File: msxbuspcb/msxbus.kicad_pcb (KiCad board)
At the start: 2 copper layers, 9 parts, among them J1 RPi_GPIO, P1 CONN_02X25, P2 CONN_02X25, P4 CONN_01X03, U1 EMP240

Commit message: route for pcb
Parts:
- added P3: CONN_02X05, Pin_Headers:Pin_Header_Straight_2x05, F.Cu at (167.6, 100.4)
- R1, R2, R3, R4: footprint Resistors_SMD:R_2010_HandSoldering -> Resistors_SMD:R_0603_HandSoldering
- moved R1 15.7 mm to (168.9, 97.2)
- moved R2 15.0 mm to (173.3, 100.9), turned to 270 degrees
- moved R3 14.2 mm to (173.3, 105.6), turned to 90 degrees
- moved R4 13.5 mm to (173.4, 110.4), turned to 270 degrees
- moved P4 2.36 mm to (110.5, 94.0)
- moved U1 2.34 mm to (143.3, 105.9)
- moved P2 1.80 mm to (172.1, 146.7)
- moved P1 1.80 mm to (172.1, 125.1)
- moved J1 0.90 mm to (167.6, 80.0)
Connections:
- net /3V3 renamed +3V3
- net /CLK3 renamed Net-(U1-Pad64)
- J1 pad 15: /SLTSL1 -> /MSLTSL1
- U1 pad 100: /SLTSL0 -> /SLTSL1
- U1 pad 30: /MD11 -> Net-(U1-Pad30)
- U1 pad 33: /MD08 -> /MD11
- U1 pad 34: /MD11 -> /MD08
- U1 pad 49: Net-(U1-Pad49) -> /SW2
- U1 pad 50: Net-(U1-Pad50) -> /SW1
- U1 pad 51: /SW2 -> /SWOUT
- U1 pad 52: /SW1 -> /CLOCK
- U1 pad 53: /SWOUT -> /D7
- U1 pad 54: /D7 -> /D6
- U1 pad 55: /D6 -> /D5
- U1 pad 56: /D5 -> /D4
- U1 pad 57: /D4 -> /D3
- U1 pad 58: /D3 -> /D2
- U1 pad 61: /D2 -> /D1
- U1 pad 62: /CLOCK -> /D0
- U1 pad 66: /D1 -> /A5
- U1 pad 67: /D0 -> /A4
- U1 pad 68: /A5 -> /A3
- U1 pad 97: /CS1 -> /SLTSL0
- U1 pad 98: /CS2 -> /CS1
- U1 pad 99: /SLTSL1 -> /CS2
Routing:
- net +3V3: track 0.00 -> 159.3 mm, vias 0 -> 3
- net +5V: track 0.00 -> 149.4 mm
- net /SW2: track 0.00 -> 69.8 mm
- net /SLTSL1: track 0.00 -> 63.2 mm
- net Net-(P2-Pad49): track 0.00 -> 58.9 mm
- net /CS2: track 0.00 -> 56.9 mm
- net /CS1: track 0.00 -> 52.0 mm
- net /RFSH: track 0.00 -> 51.3 mm
- net /CS12: track 0.00 -> 49.5 mm
- net /INT: track 0.00 -> 49.4 mm
- net /CLOCK: track 0.00 -> 48.6 mm
- net /D6: track 0.00 -> 47.2 mm
- net /BUSDIR: track 0.00 -> 47.1 mm
- net /D4: track 0.00 -> 45.8 mm
- net /MERQ: track 0.00 -> 45.4 mm
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- added copper zone on F.Cu, net /GND
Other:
- board outline added: 72.4 x 77.5 mm
- net class 3V3 added: clearance 0.18, trace_width 0.2, via_dia 0.6, via_drill 0.4
- net class 5V added: clearance 0.18, trace_width 0.5, via_dia 0.6, via_drill 0.4
- net class Default: clearance 0.2 -> 0.18; trace_width 0.25 -> 0.2
- rule trace_clearance: 0.2 -> 0.18

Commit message: simple PCB added
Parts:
- added G***: LOGO, msxbuspcb:msx, F.Cu at (99.6, 123.4)
- moved R3 31.3 mm to (163.8, 75.8)
- moved U1 31.3 mm to (133.7, 76.1)
- moved J1 31.3 mm to (158.1, 50.2)
- moved P1 31.3 mm to (162.6, 95.2)
- moved P2 31.3 mm to (162.6, 116.8)
- moved P3 31.3 mm to (158.1, 70.6)
- moved P4 31.3 mm to (101.0, 64.1)
- moved R2 31.3 mm to (163.8, 71.0)
- moved R4 31.3 mm to (163.9, 80.6)
- moved R1 31.3 mm to (159.3, 67.4)
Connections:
- net Net-(P1-Pad49) renamed /SOUNDIN1
- net Net-(P2-Pad49) renamed /SOUNDIN0
- J1 pad 14: /GND -> GND
- J1 pad 20: /GND -> GND
- J1 pad 25: /GND -> GND
- J1 pad 30: /GND -> GND
- J1 pad 34: /GND -> GND
- J1 pad 39: /GND -> GND
- J1 pad 6: /GND -> GND
- J1 pad 9: /GND -> GND
- P1 pad 41: /GND -> GND
- P1 pad 43: /GND -> GND
- P1 pad 47: Net-(P1-Pad47) -> +5V
- P2 pad 41: /GND -> GND
- P2 pad 43: /GND -> GND
- P2 pad 47: Net-(P2-Pad47) -> +5V
- P3 pad 10: /GND -> GND
- P3 pad 2: /GND -> GND
- P4 pad 2: /GND -> GND
- U1 pad 10: /GND -> GND
- U1 pad 11: +3V3 -> GND
- U1 pad 32: /GND -> GND
- U1 pad 46: /GND -> GND
- U1 pad 60: /GND -> GND
- U1 pad 65: /GND -> GND
- U1 pad 79: /GND -> GND
- U1 pad 8: +3V3 -> Net-(U1-Pad8)
- U1 pad 9: /GND -> +3V3
- U1 pad 93: /GND -> GND
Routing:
- net GND: track 0.00 -> 36.2 mm, vias 0 -> 6
- net /SWOUT: track 27.2 -> 49.8 mm
- net +3V3: track 159.3 -> 171.0 mm, vias 3 -> 2
- net +5V: track 149.4 -> 152.8 mm
- added copper zone on B.Cu, net GND
- added copper zone on F.Cu, net GND
- removed copper zone on F.Cu, net /GND
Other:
- board size 72.4 x 77.5 mm -> 76.7 x 80 mm
- board text added: "RPMC Slot Test V0.5 2016.03.15"
- board text added: "meeso.kim@gmail.com"

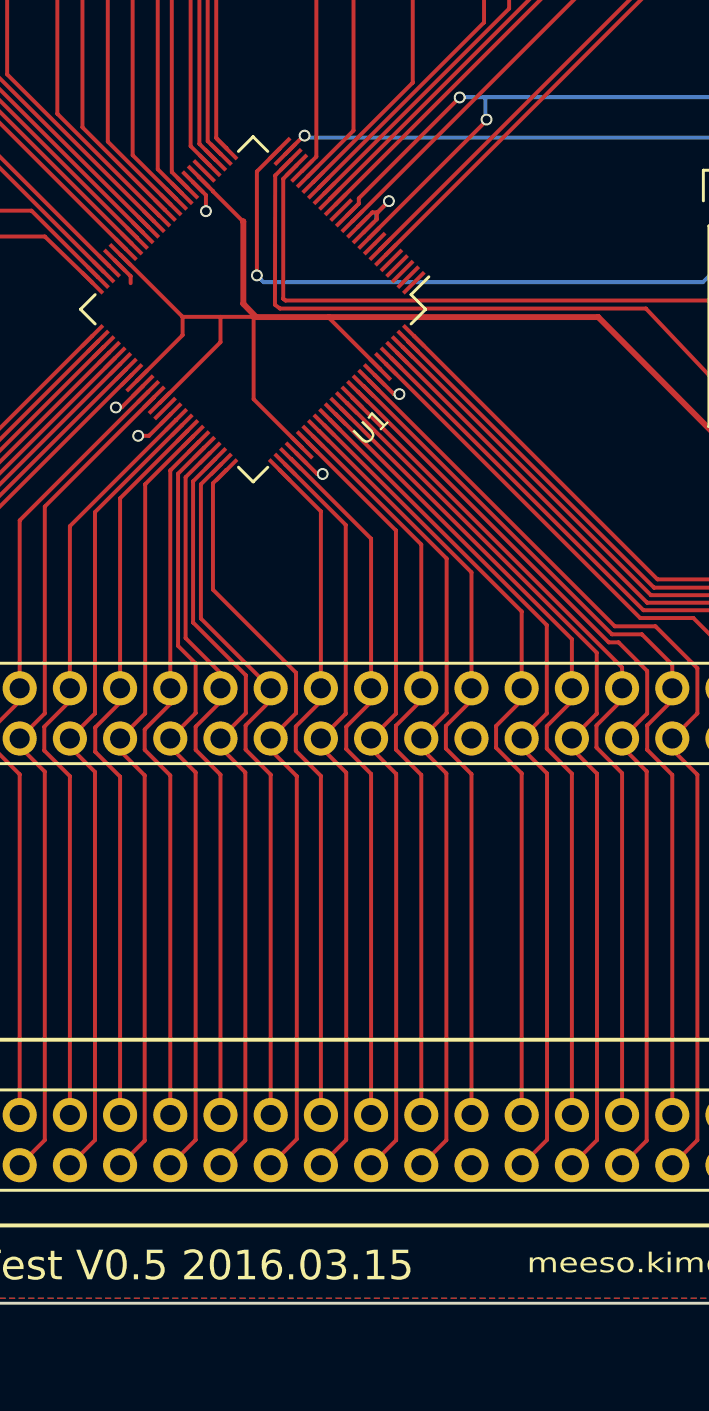
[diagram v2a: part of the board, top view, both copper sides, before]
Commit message: capacitors added
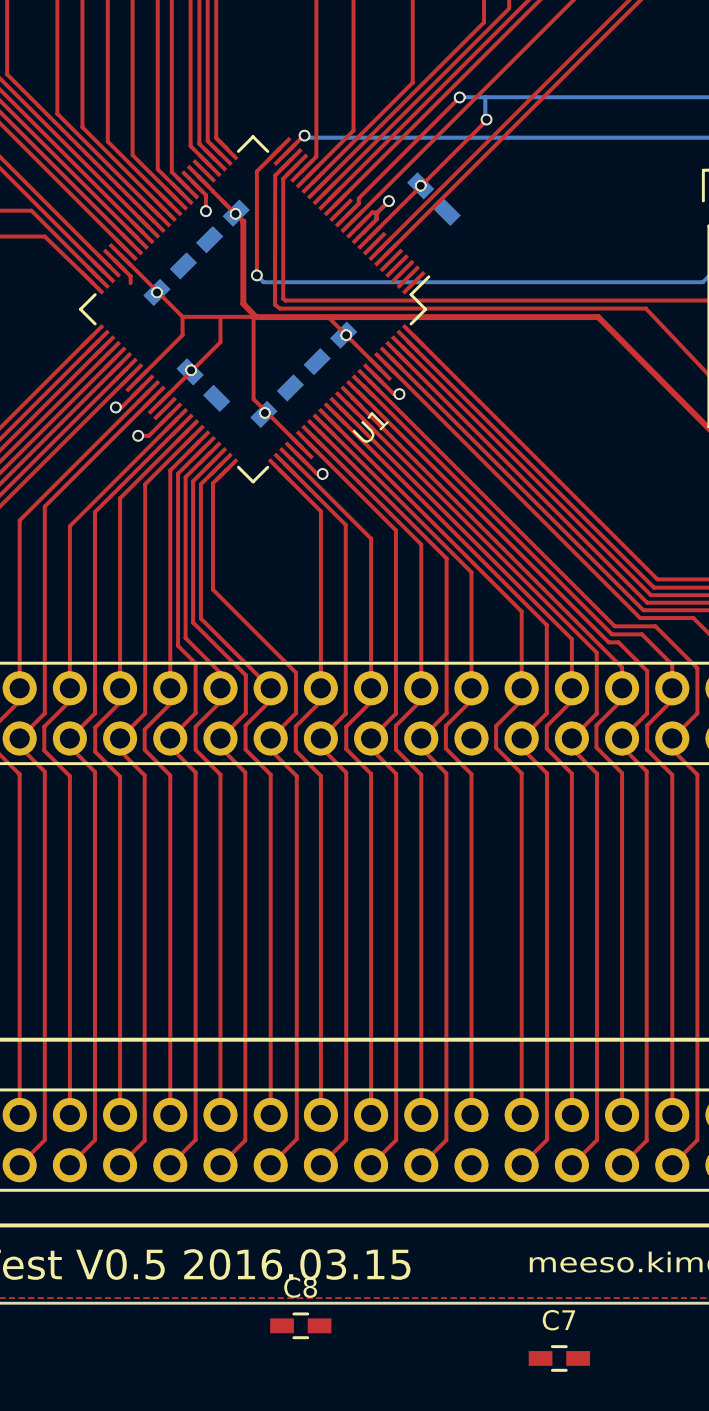
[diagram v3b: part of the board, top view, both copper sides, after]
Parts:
- added C1: 104, Capacitors_SMD:C_0603_HandSoldering, B.Cu at (132.2, 71.9)
- added C2: C, Capacitors_SMD:C_0603_HandSoldering, B.Cu at (129.5, 74.5)
- added C3: C, Capacitors_SMD:C_0603_HandSoldering, B.Cu at (135.0, 80.7)
- added C4: C, Capacitors_SMD:C_0603_HandSoldering, B.Cu at (131.2, 79.9)
- added C5: 104, Capacitors_SMD:C_0603_HandSoldering, B.Cu at (137.6, 78.1)
- added C6: C, Capacitors_SMD:C_0603_HandSoldering, B.Cu at (142.9, 70.5)
- added C7: C, Capacitors_SMD:C_0603_HandSoldering, F.Cu at (149.2, 129.2)
- added C8: C, Capacitors_SMD:C_0603_HandSoldering, F.Cu at (136.1, 127.5)
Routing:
- net +3V3: track 171.0 -> 172.4 mm, vias 2 -> 8

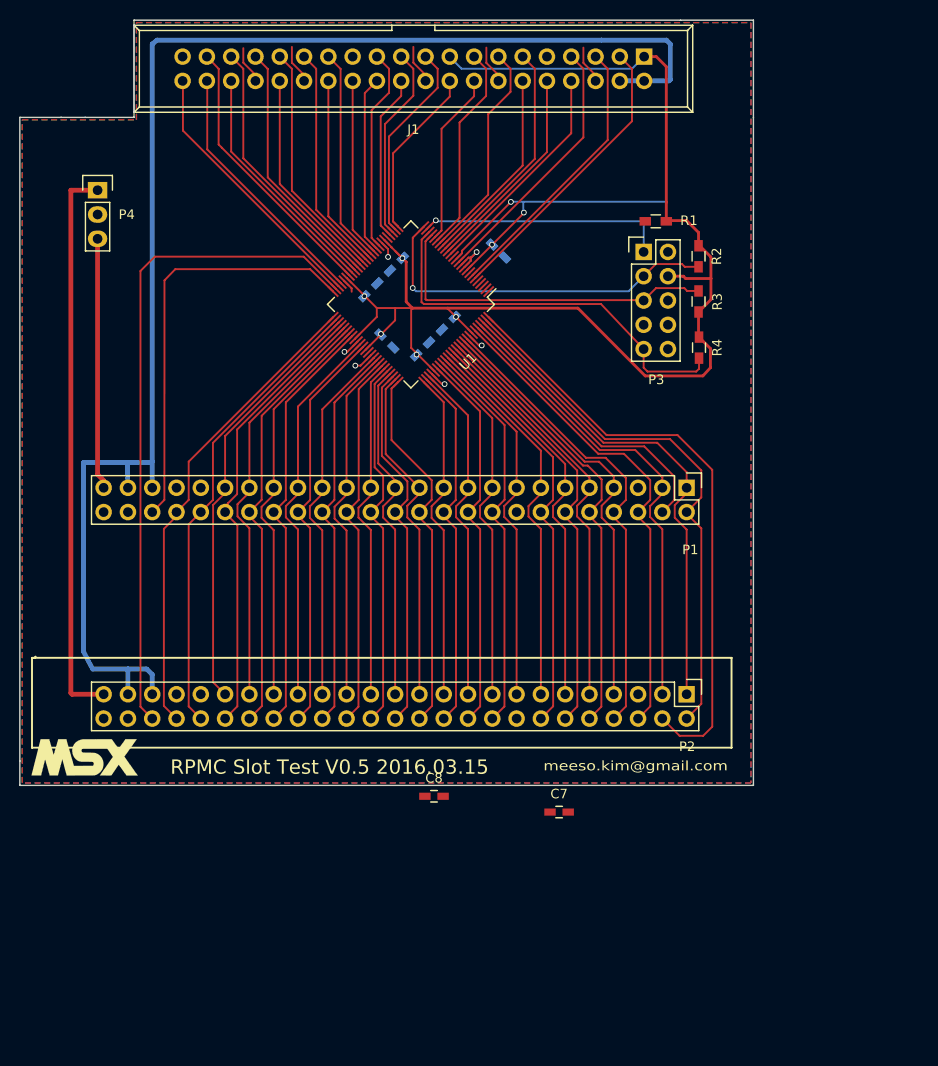
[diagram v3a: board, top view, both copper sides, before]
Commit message: epm240 12mm to 14mm
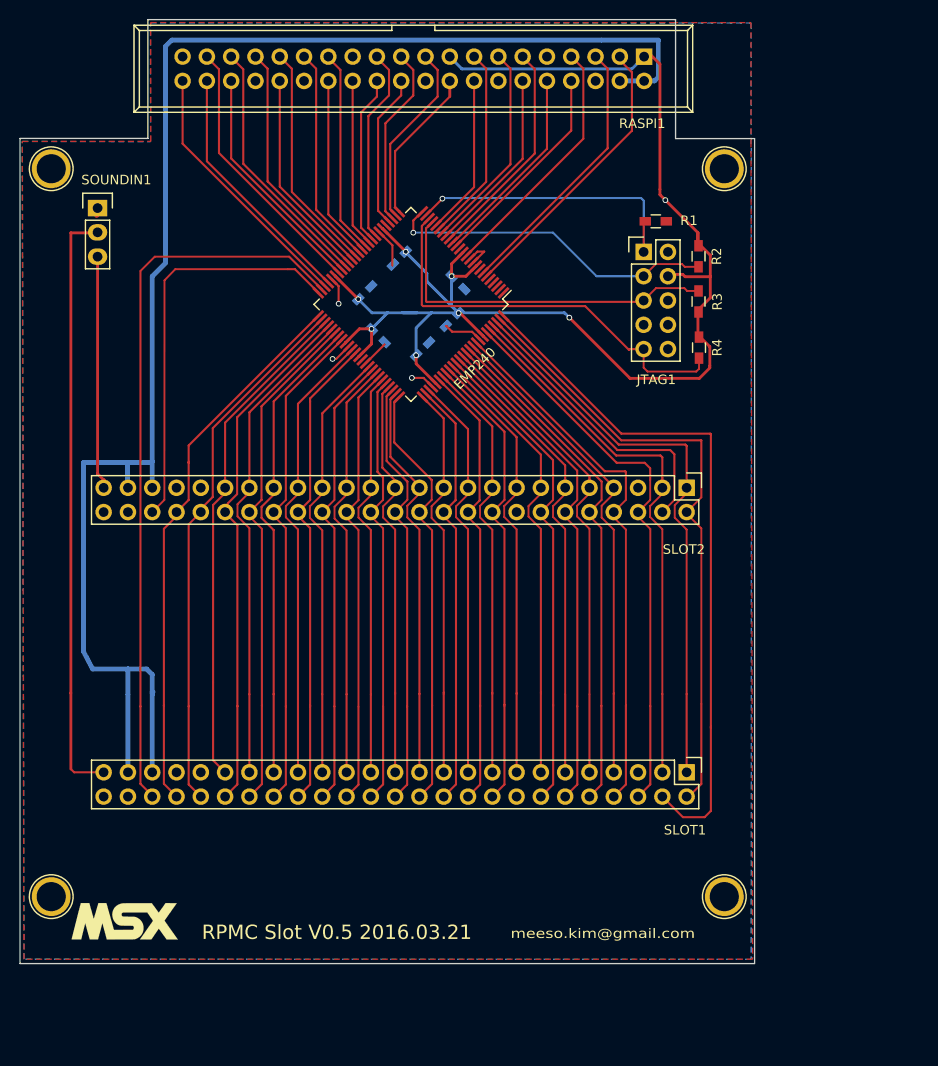
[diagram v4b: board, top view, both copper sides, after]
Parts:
- removed C7, C8: C, Capacitors_SMD:C_0603_HandSoldering
- added REF**: 1pin, Connect:1pin, F.Cu at (166.5, 61.9)
- added REF**: 1pin, Connect:1pin, F.Cu at (96.1, 61.9)
- added REF**: 1pin, Connect:1pin, F.Cu at (166.5, 138.0)
- added REF**: 1pin, Connect:1pin, F.Cu at (96.1, 138.0)
- ?: renamed from G***; value LOGO -> (none)
- C1, C5: value 104 -> C
- EMP240: renamed from U1; footprint Housings_QFP:TQFP-100_12x12mm_Pitch0.4mm -> Housings_QFP:TQFP-100_14x14mm_Pitch0.5mm
- moved ? 17.6 mm to (103.8, 140.6)
- moved SLOT1 8.16 mm to (162.6, 125.0)
- moved C6 5.37 mm to (138.7, 73.8)
- moved SOUNDIN1 1.86 mm to (101.0, 66.0)
- moved C4 1.06 mm to (130.3, 79.3)
- moved C1 0.72 mm to (132.5, 71.2)
- moved C2 0.71 mm to (128.9, 74.9)
- moved C5 0.57 mm to (138.0, 77.7)
- renumbered P3 to JTAG1, J1 to RASPI1, P2 to SLOT1, P1 to SLOT2, P4 to SOUNDIN1
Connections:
- R1 pad 1: +3V3 -> GND
- SOUNDIN1 pad 1: /SOUNDIN0 -> GND
- SOUNDIN1 pad 2: GND -> /SOUNDIN0
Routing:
- net +3V3: track 172.4 -> 154.3 mm
- net +5V: track 152.8 -> 166.2 mm
- net GND: track 36.2 -> 23.8 mm, vias 6 -> 3
- net /SLTSL1: track 63.2 -> 72.6 mm
- net /CS12: track 49.5 -> 58.7 mm
- net /CS2: track 56.9 -> 65.6 mm
- net /CS1: track 52.0 -> 60.4 mm
- net /M1: track 43.0 -> 51.3 mm
- net /SWOUT: track 49.8 -> 57.7 mm
- net /CLOCK: track 48.6 -> 56.2 mm
- net /RFSH: track 51.3 -> 58.9 mm
- net /D7: track 44.8 -> 52.4 mm
- net /D4: track 45.8 -> 53.4 mm
- net /D6: track 47.2 -> 54.8 mm
- net /D5: track 43.4 -> 50.9 mm
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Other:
- board size 76.7 x 80 mm -> 76.8 x 98.7 mm
- net class 3V3: trace_width 0.2 -> 0.3
- net class Default: trace_width 0.2 -> 0.22
- net class SOUND added: clearance 0.18, trace_width 0.3, via_dia 0.6, via_drill 0.4
- board text added: "RPMC Slot V0.5 2016.03.21"
- board text removed: "RPMC Slot Test V0.5 2016.03.15"
